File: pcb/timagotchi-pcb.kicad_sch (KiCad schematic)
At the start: 8 parts, among them SW1 SW_Push, SW2 SW_Push

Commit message: new kicad version did stuff to the schematic for whatever reason
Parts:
- Brd1: value (none) -> SSD1306; footprint (none) -> Display:Adafruit_SSD1306_No_Mounting_Holes
- R1, R2: value (none) -> 10k; footprint (none) -> Resistor_SMD:R_0805_2012Metric
- R3: value (none) -> 3.3k; footprint (none) -> Resistor_SMD:R_0805_2012Metric
- SW1, SW2: footprint (none) -> Button_Switch_THT:SW_PUSH_6mm
- SW3: value (none) -> SW_Push; footprint (none) -> Button_Switch_THT:SW_PUSH_6mm
- U1: value (none) -> Arduino_Nano; footprint (none) -> Arduino:Arduino_Nano
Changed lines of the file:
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@@
       (effects (font (size 1.27 1.27)) hide)
     )
-    (property "Value" "" (id 1) (at 164.465 87.6299 90)
+    (property "Value" "+5V" (id 1) (at 164.465 87.6299 90)
       (effects (font (size 1.27 1.27)) (justify left))
     )
@@
       (effects (font (size 1.27 1.27)) hide)
     )
-    (property "Value" "" (id 1) (at 179.705 102.8699 90)
+    (property "Value" "+5V" (id 1) (at 179.705 102.8699 90)
       (effects (font (size 1.27 1.27)) (justify left))
     )
@@
       (effects (font (size 1.27 1.27)) hide)
     )
-    (property "Value" "" (id 1) (at 158.75 65.405 0))
+    (property "Value" "+BATT" (id 1) (at 158.75 65.405 0))
     (property "Footprint" "" (id 2) (at 163.195 65.405 0)
       (effects (font (size 1.27 1.27)) hide)
@@
       (effects (font (size 1.27 1.27)) hide)
     )
-    (property "Value" "" (id 1) (at 168.91 68.5799 90)
+    (property "Value" "PWR_FLAG" (id 1) (at 168.91 68.5799 90)
       (effects (font (size 1.27 1.27)) (justify left))
     )
@@
     (property "Reference" "SW2" (id 0) (at 100.965 102.235 0))
     (property "Value" "SW_Push" (id 1) (at 100.965 108.585 0))
-    (property "Footprint" "" (id 2) (at 100.965 101.6 0)
+    (property "Footprint" "Button_Switch_THT:SW_PUSH_6mm" (id 2) (at 100.965 101.6 0)
       (effects (font (size 1.27 1.27)) hide)
     )
@@
       (effects (font (size 1.27 1.27)) (justify left))
     )
-    (property "Value" "" (id 1) (at 106.045 92.71 90)
-      (effects (font (size 1.27 1.27)) (justify left))
-    )
-    (property "Footprint" "" (id 2) (at 107.823 90.805 90)
+    (property "Value" "10k" (id 1) (at 106.045 92.71 90)
+      (effects (font (size 1.27 1.27)) (justify left))
+    )
+    (property "Footprint" "Resistor_SMD:R_0805_2012Metric" (id 2) (at 107.823 90.805 90)
       (effects (font (size 1.27 1.27)) hide)
     )
@@
       (effects (font (size 1.27 1.27)) (justify left))
     )
-    (property "Value" "" (id 1) (at 183.515 80.645 90)
-      (effects (font (size 1.27 1.27)) (justify left))
-    )
-    (property "Footprint" "" (id 2) (at 181.737 78.74 90)
+    (property "Value" "3.3k" (id 1) (at 183.515 80.645 90)
+      (effects (font (size 1.27 1.27)) (justify left))
+    )
+    (property "Footprint" "Resistor_SMD:R_0805_2012Metric" (id 2) (at 181.737 78.74 90)
       (effects (font (size 1.27 1.27)) hide)
     )
@@
       (effects (font (size 1.27 1.27)) hide)
     )
-    (property "Value" "" (id 1) (at 92.71 81.2799 90)
+    (property "Value" "+5V" (id 1) (at 92.71 81.2799 90)
       (effects (font (size 1.27 1.27)) (justify left))
     )
@@
       (effects (font (size 1.27 1.27)) hide)
     )
-    (property "Value" "" (id 1) (at 160.02 68.5799 90)
+    (property "Value" "PWR_FLAG" (id 1) (at 160.02 68.5799 90)
       (effects (font (size 1.27 1.27)) (justify left))
     )
@@
     (in_bom yes) (on_board yes) (fields_autoplaced)
     (property "Reference" "U1" (id 0) (at 145.415 71.755 0))
-    (property "Value" "" (id 1) (at 145.415 74.295 0))
-    (property "Footprint" "" (id 2) (at 145.415 119.38 0)
+    (property "Value" "Arduino_Nano" (id 1) (at 145.415 74.295 0))
+    (property "Footprint" "Arduino:Arduino_Nano" (id 2) (at 145.415 119.38 0)
       (effects (font (size 1.27 1.27)) hide)
     )
@@
     (in_bom yes) (on_board yes)
     (property "Reference" "SW3" (id 0) (at 191.77 80.645 0))
-    (property "Value" "" (id 1) (at 191.77 86.995 0))
-    (property "Footprint" "" (id 2) (at 191.77 80.01 0)
+    (property "Value" "SW_Push" (id 1) (at 191.77 86.995 0))
+    (property "Footprint" "Button_Switch_THT:SW_PUSH_6mm" (id 2) (at 191.77 80.01 0)
       (effects (font (size 1.27 1.27)) hide)
     )
@@
       (effects (font (size 1.27 1.27)) hide)
     )
-    (property "Value" "" (id 1) (at 183.515 69.215 0))
+    (property "Value" "+5V" (id 1) (at 183.515 69.215 0))
     (property "Footprint" "" (id 2) (at 183.515 74.93 0)
       (effects (font (size 1.27 1.27)) hide)
@@
       (effects (font (size 1.27 1.27)) hide)
     )
-    (property "Value" "" (id 1) (at 92.71 106.6799 90)
+    (property "Value" "+5V" (id 1) (at 92.71 106.6799 90)
       (effects (font (size 1.27 1.27)) (justify left))
     )
@@
       (effects (font (size 1.27 1.27)) hide)
     )
-    (property "Value" "" (id 1) (at 172.72 80.0099 90)
+    (property "Value" "+9V" (id 1) (at 172.72 80.0099 90)
       (effects (font (size 1.27 1.27)) (justify left))
     )
@@
       (effects (font (size 1.27 1.27)) (justify left))
     )
-    (property "Value" "" (id 1) (at 106.045 118.11 90)
-      (effects (font (size 1.27 1.27)) (justify left))
-    )
-    (property "Footprint" "" (id 2) (at 107.823 116.205 90)
+    (property "Value" "10k" (id 1) (at 106.045 118.11 90)
+      (effects (font (size 1.27 1.27)) (justify left))
+    )
+    (property "Footprint" "Resistor_SMD:R_0805_2012Metric" (id 2) (at 107.823 116.205 90)
       (effects (font (size 1.27 1.27)) hide)
     )
@@
       (effects (font (size 1.27 1.27)) hide)
     )
-    (property "Value" "" (id 1) (at 126.365 87.6299 90)
+    (property "Value" "GND" (id 1) (at 126.365 87.6299 90)
       (effects (font (size 1.27 1.27)) (justify right))
     )
@@
       (effects (font (size 1.27 1.27)) hide)
     )
-    (property "Value" "" (id 1) (at 183.515 108.585 0))
+    (property "Value" "GND" (id 1) (at 183.515 108.585 0))
     (property "Footprint" "" (id 2) (at 183.515 105.41 0)
       (effects (font (size 1.27 1.27)) hide)
@@
     (property "Reference" "SW1" (id 0) (at 100.965 76.835 0))
     (property "Value" "SW_Push" (id 1) (at 100.965 83.185 0))
-    (property "Footprint" "" (id 2) (at 100.965 76.2 0)
+    (property "Footprint" "Button_Switch_THT:SW_PUSH_6mm" (id 2) (at 100.965 76.2 0)
       (effects (font (size 1.27 1.27)) hide)
     )
@@
       (effects (font (size 1.27 1.27)) hide)
     )
-    (property "Value" "" (id 1) (at 106.045 99.06 0))
+    (property "Value" "GND" (id 1) (at 106.045 99.06 0))
     (property "Footprint" "" (id 2) (at 106.045 94.615 0)
       (effects (font (size 1.27 1.27)) hide)
@@
       (effects (font (size 1.27 1.27)) hide)
     )
-    (property "Value" "" (id 1) (at 169.545 65.405 0))
+    (property "Value" "-BATT" (id 1) (at 169.545 65.405 0))
     (property "Footprint" "" (id 2) (at 165.735 65.405 0)
       (effects (font (size 1.27 1.27)) hide)
@@
       (effects (font (size 1.27 1.27)) hide)
     )
-    (property "Value" "" (id 1) (at 173.355 82.5499 90)
+    (property "Value" "GND" (id 1) (at 173.355 82.5499 90)
       (effects (font (size 1.27 1.27)) (justify right))
     )
@@
       (effects (font (size 1.27 1.27)) (justify right))
     )
-    (property "Value" "" (id 1) (at 191.1351 108.585 0)
-      (effects (font (size 1.27 1.27)) (justify right))
-    )
-    (property "Footprint" "" (id 2) (at 186.055 101.6 0)
-      (effects (font (size 1.27 1.27)) hide)
-    )
+    (property "Value" "SSD1306" (id 1) (at 191.1351 108.585 0)
+      (effects (font (size 1.27 1.27)) (justify right))
+    )
+    (property "Footprint" "Display:Adafruit_SSD1306_No_Mounting_Holes" (id 2) (at 186.055 101.6 0)
+      (effects (font (size 1.27 1.27)) hide)
+    )

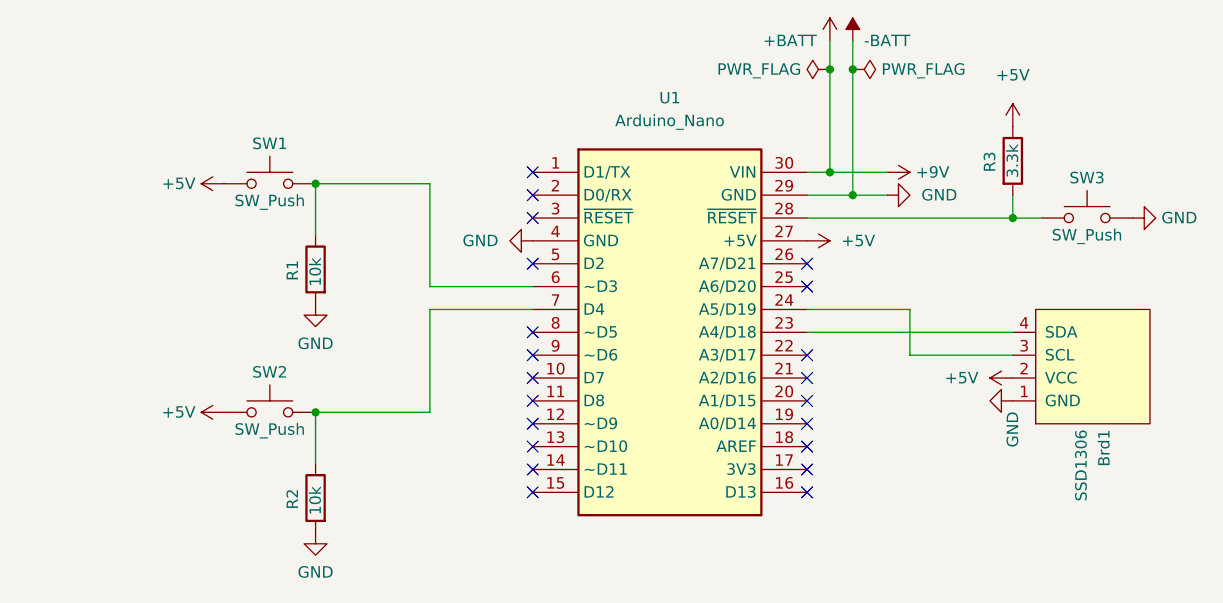
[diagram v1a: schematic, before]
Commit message: schematic v2
switch to pro micro 3.3v
* will be able to tune power lower
* smaller footprint

add third button

change buttons from pulldown to pullup
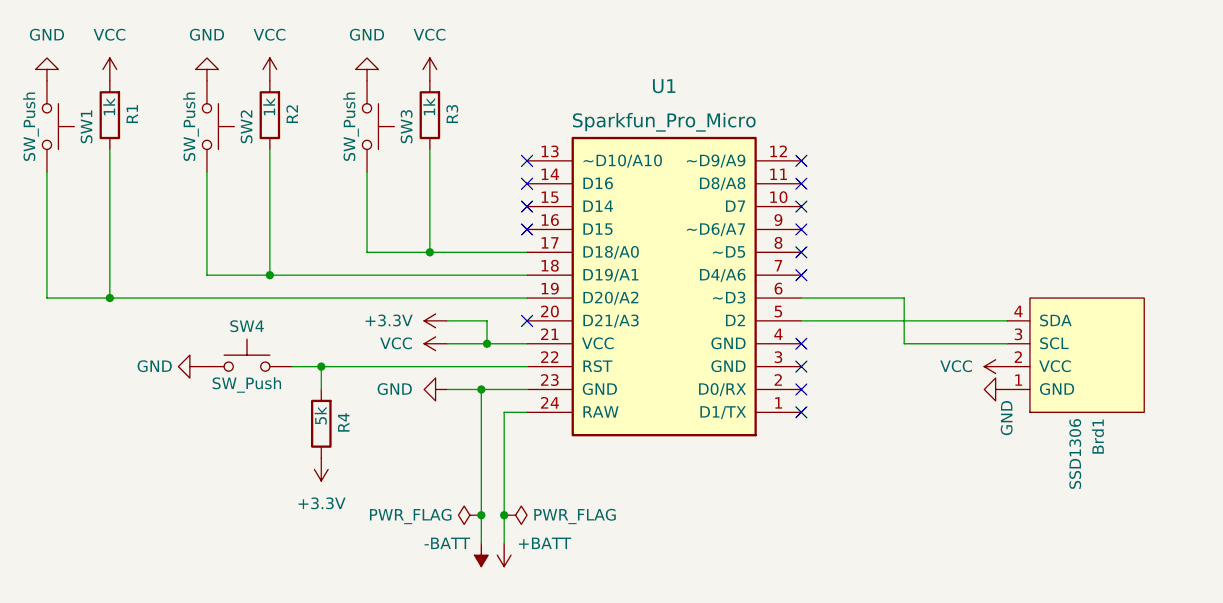
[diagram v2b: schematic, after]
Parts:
- removed SW3: SW_Push, Button_Switch_THT:SW_PUSH_6mm, symbol Switch:SW_Push
- removed U1: Arduino_Nano, Arduino:Arduino_Nano, symbol Arduino:Arduino_Nano
- added R3: 1k, Resistor_SMD:R_0805_2012Metric, symbol Device:R
- added SW1, SW4: SW_Push, Button_Switch_THT:SW_PUSH_6mm, symbol Switch:SW_Push
- added U1: Sparkfun_Pro_Micro, Arduino:Sparkfun_Pro_Micro, symbol Arduino:Sparkfun_Pro_Micro
- R1, R2: value 10k -> 1k
- R4: renamed from R3; value 3.3k -> 5k
- renumbered SW1 to SW3
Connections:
- net -BATT: now also SW2.2, SW3.2, SW1.2, SW4.2, U1.23 (GND); no longer R1.2, R2.2
- net at R2.1, SW2.1: now also U1.18 (D19/A1)
- net at R1.1: now also SW1.1, U1.19 (D20/A2); no longer SW3.1
- net at R4.2: now also SW4.1, U1.22 (RST)
- net at Brd1.4 (SDA): now also U1.5 (D2)
- net at Brd1.3 (SCL): now also U1.6 (~D3)
- net +5V renamed +3V3
- net +3V3: now also R1.2, R2.2, R3.2, U1.21 (VCC); no longer SW2.2, SW3.2
- new net: R3.1, SW3.1, U1.17 (D18/A0)
- new net +BATT: U1.24 (RAW)
- no-connect marks 21 -> 15
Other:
- moved on the sheet: Brd1, R4, SW3

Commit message: add missing pwr_flag
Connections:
- net +3V3 renamed VCC
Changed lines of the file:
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@@
-    (pin "1")
-  )
-  (symbol (lib_id "power:+3.3V") (at 106.68 111.76 180) (unit 1)
-    (in_bom yes) (on_board yes) (fields_autoplaced)
-    (property "Reference" "#PWR013" (id 0) (at 106.68 107.95 0)
-      (effects (font (size 1.27 1.27)) hide)
-    )
-    (property "Value" "+3.3V" (id 1) (at 106.68 116.84 0))
-    (property "Footprint" "" (id 2) (at 106.68 111.76 0)
-      (effects (font (size 1.27 1.27)) hide)
-    )
-    (property "Datasheet" "" (id 3) (at 106.68 111.76 0)
-      (effects (font (size 1.27 1.27)) hide)
-    )
     (pin "1")
   )
@@
     (pin "1")
   )
+  (symbol (lib_id "power:PWR_FLAG") (at 120.65 96.52 90) (unit 1)
+    (in_bom yes) (on_board yes) (fields_autoplaced)
+    (property "Reference" "#FLG0101" (id 0) (at 118.745 96.52 0)
+      (effects (font (size 1.27 1.27)) hide)
+    )
+    (property "Value" "PWR_FLAG" (id 1) (at 116.84 96.5199 90)
+      (effects (font (size 1.27 1.27)) (justify left))
+    )
+    (property "Footprint" "" (id 2) (at 120.65 96.52 0)
+      (effects (font (size 1.27 1.27)) hide)
+    )
+    (property "Datasheet" "~" (id 3) (at 120.65 96.52 0)
+      (effects (font (size 1.27 1.27)) hide)
+    )
+    (pin "1")
+  )
   (symbol (lib_id "Switch:SW_Push") (at 111.76 74.93 270) (mirror x) (unit 1)
     (in_bom yes) (on_board yes)
@@
     (pin "2")
   )
+  (symbol (lib_id "power:VCC") (at 106.68 111.76 180) (unit 1)
+    (in_bom yes) (on_board yes) (fields_autoplaced)
+    (property "Reference" "#PWR0101" (id 0) (at 106.68 107.95 0)
+      (effects (font (size 1.27 1.27)) hide)
+    )
+    (property "Value" "VCC" (id 1) (at 106.68 116.84 0))
+    (property "Footprint" "" (id 2) (at 106.68 111.76 0)
+      (effects (font (size 1.27 1.27)) hide)
+    )
+    (property "Datasheet" "" (id 3) (at 106.68 111.76 0)
+      (effects (font (size 1.27 1.27)) hide)
+    )
+    (pin "1")
+  )
   (symbol (lib_id "power:-BATT") (at 124.46 121.285 180) (unit 1)
     (in_bom yes) (on_board yes)
@@
     )
     (property "Datasheet" "" (id 3) (at 76.2 69.85 0)
-      (effects (font (size 1.27 1.27)) hide)
-    )
-    (pin "1")
-  )
-  (symbol (lib_id "power:+3.3V") (at 120.65 96.52 90) (unit 1)
-    (in_bom yes) (on_board yes) (fields_autoplaced)
-    (property "Reference" "#PWR07" (id 0) (at 124.46 96.52 0)
-      (effects (font (size 1.27 1.27)) hide)
-    )
-    (property "Value" "+3.3V" (id 1) (at 116.84 96.5199 90)
-      (effects (font (size 1.27 1.27)) (justify left))
-    )
-    (property "Footprint" "" (id 2) (at 120.65 96.52 0)
-      (effects (font (size 1.27 1.27)) hide)
-    )
-    (property "Datasheet" "" (id 3) (at 120.65 96.52 0)
       (effects (font (size 1.27 1.27)) hide)
     )
@@
       (reference "#FLG02") (unit 1) (value "PWR_FLAG") (footprint "")
     )
+    (path "/b258beff-21a6-4047-b135-54bb1952210f"
+      (reference "#FLG0101") (unit 1) (value "PWR_FLAG") (footprint "")
+    )
     (path "/ea4f8155-bb3d-45e0-94b0-ce6059436d00"
       (reference "#PWR01") (unit 1) (value "GND") (footprint "")
@@
       (reference "#PWR06") (unit 1) (value "VCC") (footprint "")
     )
-    (path "/f5e39e67-7f99-44fe-bcad-7a58d93a6b20"
-      (reference "#PWR07") (unit 1) (value "+3.3V") (footprint "")
-    )
     (path "/9db3a35b-5234-4c91-bad4-e488926b30db"
       (reference "#PWR08") (unit 1) (value "VCC") (footprint "")
@@
       (reference "#PWR012") (unit 1) (value "GND") (footprint "")
     )
-    (path "/13171f30-b0b6-45c3-a90e-f90091f5761a"
-      (reference "#PWR013") (unit 1) (value "+3.3V") (footprint "")
-    )
     (path "/c00190dc-5154-4ae0-afa2-421e4cfffcf8"
       (reference "#PWR014") (unit 1) (value "-BATT") (footprint "")
@@
       (reference "#PWR015") (unit 1) (value "+BATT") (footprint "")
     )
+    (path "/b6e3d76e-c56a-471c-922c-7e3334a163d0"
+      (reference "#PWR0101") (unit 1) (value "VCC") (footprint "")
+    )
     (path "/f641e724-f6c6-4cc1-9573-a10a2c206448"

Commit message: balance resistors and gen new pcb
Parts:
- R1, R2, R3: value 1k -> 3.3k
- R4: value 5k -> 3.3k
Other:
- title: (none) -> "Timagotchi"
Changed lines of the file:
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@@
 (kicad_sch (version 20211123) (generator eeschema)
   (paper "A4")
+  (title_block
+    (title "\"Timagotchi\"")
+    (date "2022-05-31")
+    (rev "v2")
+  )
   (junction (at 83.185 93.98) (diameter 0) (color 0 0 0 0)
   )
@@
       (effects (font (size 1.27 1.27)) (justify left))
     )
-    (property "Value" "1k" (id 1) (at 100.965 71.755 90)
+    (property "Value" "3.3k" (id 1) (at 100.965 71.755 90)
       (effects (font (size 1.27 1.27)) (justify left))
     )
@@
       (effects (font (size 1.27 1.27)) (justify left))
     )
-    (property "Value" "1k" (id 1) (at 83.185 71.755 90)
+    (property "Value" "3.3k" (id 1) (at 83.185 71.755 90)
       (effects (font (size 1.27 1.27)) (justify left))
     )
@@
       (effects (font (size 1.27 1.27)) (justify left))
     )
-    (property "Value" "1k" (id 1) (at 118.745 71.755 90)
+    (property "Value" "3.3k" (id 1) (at 118.745 71.755 90)
       (effects (font (size 1.27 1.27)) (justify left))
     )
@@
       (effects (font (size 1.27 1.27)) (justify left))
     )
-    (property "Value" "5k" (id 1) (at 106.68 106.045 90)
+    (property "Value" "3.3k" (id 1) (at 106.68 106.045 90)
       (effects (font (size 1.27 1.27)) (justify left))
     )
@@
     )
     (path "/2c87f91d-a402-409c-b983-29ada36b1ee8"
-      (reference "R1") (unit 1) (value "1k") (footprint "Resistor_SMD:R_0805_2012Metric")
+      (reference "R1") (unit 1) (value "3.3k") (footprint "Resistor_SMD:R_0805_2012Metric")
     )
     (path "/14050b08-6e5e-4822-9c75-fd99029152db"
-      (reference "R2") (unit 1) (value "1k") (footprint "Resistor_SMD:R_0805_2012Metric")
+      (reference "R2") (unit 1) (value "3.3k") (footprint "Resistor_SMD:R_0805_2012Metric")
     )
     (path "/39457c37-2387-400b-b450-0cfa75ee2254"
-      (reference "R3") (unit 1) (value "1k") (footprint "Resistor_SMD:R_0805_2012Metric")
+      (reference "R3") (unit 1) (value "3.3k") (footprint "Resistor_SMD:R_0805_2012Metric")
     )
     (path "/4c75cda5-afbb-4d0c-962d-0a937dfefcf6"
-      (reference "R4") (unit 1) (value "5k") (footprint "Resistor_SMD:R_0805_2012Metric")
+      (reference "R4") (unit 1) (value "3.3k") (footprint "Resistor_SMD:R_0805_2012Metric")
     )
     (path "/4bd3ee5a-144d-43a0-809a-ca35e01fbc3a"
